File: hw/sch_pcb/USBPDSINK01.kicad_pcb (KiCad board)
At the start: 2 copper layers, 45.5 x 52.9 mm, 53 parts, among them J1 USBC_USB4105-GF-A, J2 HEADER_2x05_PARALLEL, J3 HEADER_2x04_PARALLEL, J4 HEADER_2x03_PARALLEL, J5 HEADER_2x01, J6 HEADER_2x07_PARALLEL, J7 WAGO_2604-3102, M1 HOLE, M2 HOLE, M3 HOLE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

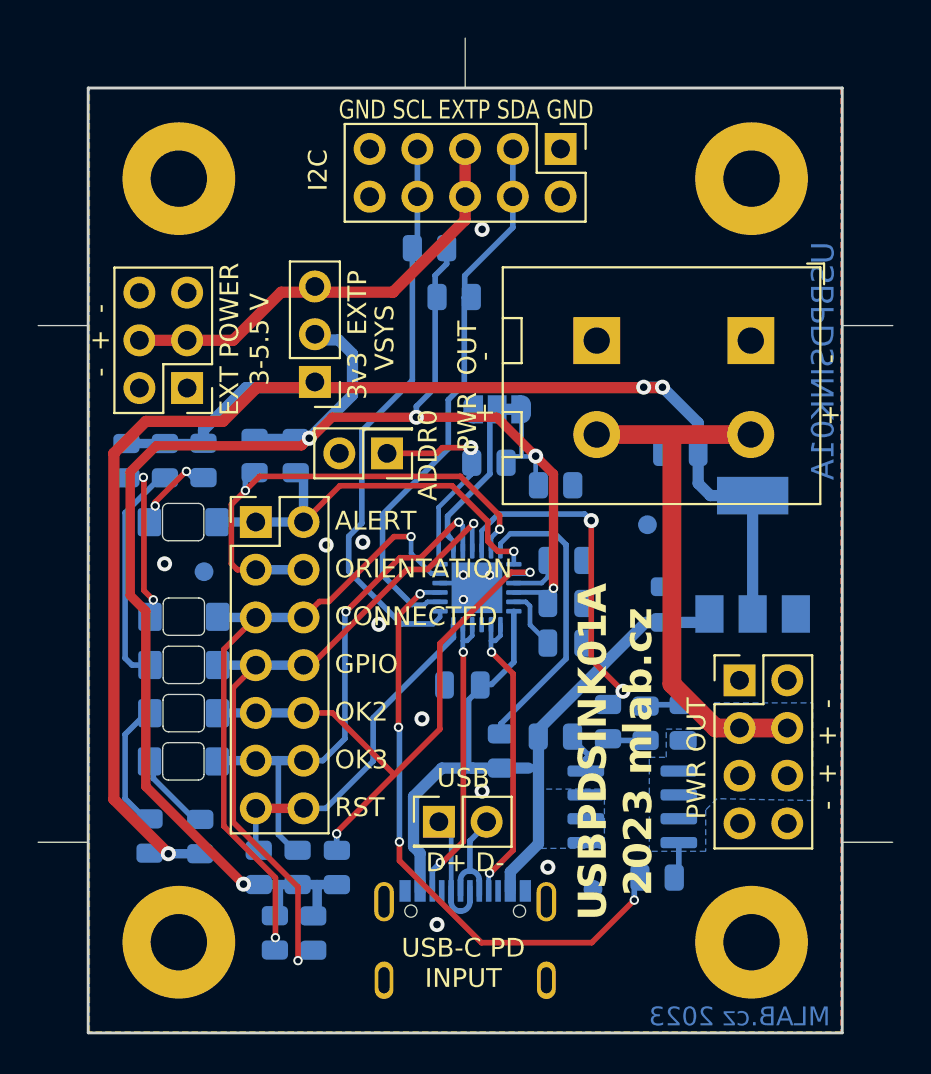
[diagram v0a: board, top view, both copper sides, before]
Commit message: add ustid, change LDO
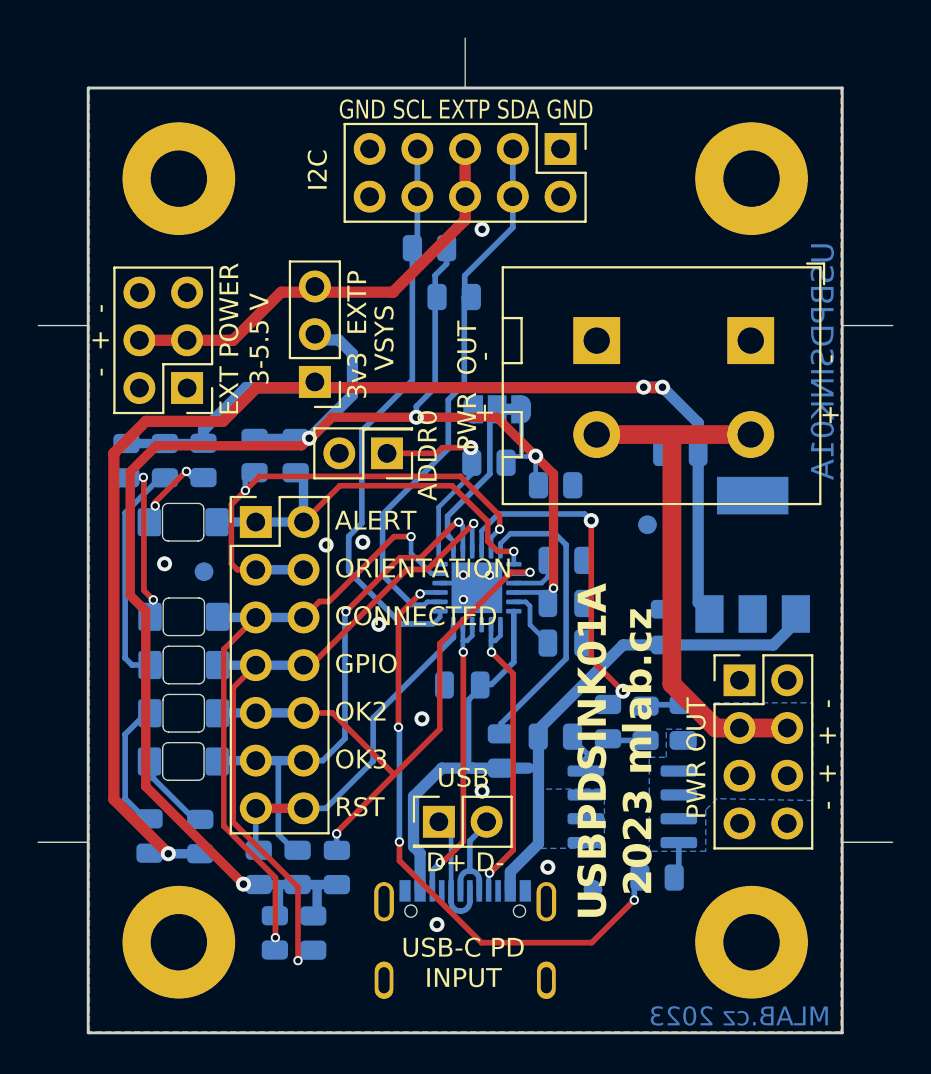
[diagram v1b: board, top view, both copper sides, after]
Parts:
- R3, R5, R6: value 65R -> 62R
- R7: value 60R -> 62R
- U2: value NCP1117-3.3 -> NCV4274CST33T3G
- moved C6 1.20 mm to (159.1, 108.5)
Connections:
- U2 pad 1: GND -> VBUS
- U2 pad 2: +3V3 -> GND
- U2 pad 3: VBUS -> +3V3
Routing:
- net VBUS: track 41.8 -> 47.1 mm
- net +3V3: track 85.3 -> 81.7 mm

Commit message: Kontrola a priprava PCB na vyrobu
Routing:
- net GND: vias 12 -> 13
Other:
- rule pad_to_mask_clearance: 0 -> 0.2
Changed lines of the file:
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@@
       (dielectric_constraints no)
     )
-    (pad_to_mask_clearance 0)
+    (pad_to_mask_clearance 0.2)
     (aux_axis_origin 123.1 135.48)
     (pcbplotparams
@@
   (via (at 141.1 104.18) (size 0.8) (drill 0.4) (layers "F.Cu" "B.Cu") (free) (net 2))
   (via (at 148.4 107.08) (size 0.5) (drill 0.3) (layers "F.Cu" "B.Cu") (net 2))
+  (via (at 149.86 107.061) (size 0.5) (drill 0.3) (layers "F.Cu" "B.Cu") (net 2))
   (via (at 148.4 105.78) (size 0.5) (drill 0.3) (layers "F.Cu" "B.Cu") (net 2))
   (via (at 149.4 117.28) (size 0.8) (drill 0.4) (layers "F.Cu" "B.Cu") (free) (net 2))
   (via (at 132.5 105.18) (size 0.8) (drill 0.4) (layers "F.Cu" "B.Cu") (free) (net 2))
   (via (at 146.2 113.43) (size 0.8) (drill 0.4) (layers "F.Cu" "B.Cu") (free) (net 2))
-  (via (at 149.8 105.78) (size 0.5) (drill 0.3) (layers "F.Cu" "B.Cu") (net 2))
+  (via (at 149.86 105.791) (size 0.5) (drill 0.3) (layers "F.Cu" "B.Cu") (net 2))
   (via (at 149.4 87.38) (size 0.8) (drill 0.4) (layers "F.Cu" "B.Cu") (free) (net 2))
   (via (at 147 124.38) (size 0.8) (drill 0.4) (layers "F.Cu" "B.Cu") (free) (net 2))
@@
   (segment (start 139.895 100.7475) (end 139.895 102.955) (width 0.5) (layer "B.Cu") (net 5))
   (segment (start 135.11 102.955) (end 139.895 102.955) (width 0.5) (layer "B.Cu") (net 5))
-  (segment (start 135.1 102.965) (end 135.11 102.955) (width 0.5) (layer "B.Cu") (net 5))
   (segment (start 151.0875 104.518) (end 151.0875 105.205) (width 0.25) (layer "B.Cu") (net 5))
   (segment (start 132 101.9) (end 133.638686 100.261314) (width 0.3) (layer "F.Cu") (net 6))
@@
   (via (at 151.9505 105.6305) (size 0.5) (drill 0.3) (layers "F.Cu" "B.Cu") (net 9))
   (segment (start 135.333332 113.115) (end 139.895 113.115) (width 0.5) (layer "B.Cu") (net 9))
-  (segment (start 141.67 120.43) (end 141.37 120.43) (width 0.3) (layer "B.Cu") (net 9))
   (segment (start 151.9505 105.6305) (end 151.876 105.705) (width 0.25) (layer "B.Cu") (net 9))
   (segment (start 135.315 113.133332) (end 135.333332 113.115) (width 0.5) (layer "B.Cu") (net 9))
@@
   (via (at 138.4 125.08) (size 0.5) (drill 0.3) (layers "F.Cu" "B.Cu") (net 13))
   (via (at 145.6182 103.7336) (size 0.5) (drill 0.3) (layers "F.Cu" "B.Cu") (net 13))
-  (segment (start 135.135 108) (end 135.17 108.035) (width 0.5) (layer "B.Cu") (net 13))
   (segment (start 138.37 125.11) (end 138.37 125.735) (width 0.3) (layer "B.Cu") (net 13))
   (segment (start 146.701992 105.705) (end 145.6182 104.621208) (width 0.25) (layer "B.Cu") (net 13))
@@
   (segment (start 140.188461 98.5075) (end 139.48 98.5075) (width 0.6) (layer "B.Cu") (net 28))
   (segment (start 142.5 94) (end 141.765 93.265) (width 0.6) (layer "B.Cu") (net 28))
-  (segment (start 147.5225 88.39) (end 147.5125 88.38) (width 0.3) (layer "B.Cu") (net 28))
   (segment (start 151.5 96.9575) (end 151.5 99.4664) (width 0.25) (layer "B.Cu") (net 28))
   (segment (start 152.25 100.75) (end 152.4 100.9) (width 0.25) (layer "B.Cu") (net 28))

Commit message: Kontrola, upravi pred vyrobou
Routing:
- net GND: vias 13 -> 14
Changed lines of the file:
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@@
   (via (at 148.4 105.78) (size 0.5) (drill 0.3) (layers "F.Cu" "B.Cu") (net 2))
   (via (at 149.4 117.28) (size 0.8) (drill 0.4) (layers "F.Cu" "B.Cu") (free) (net 2))
+  (via (at 129.921 112.1918) (size 0.8) (drill 0.4) (layers "F.Cu" "B.Cu") (free) (net 2))
   (via (at 132.5 105.18) (size 0.8) (drill 0.4) (layers "F.Cu" "B.Cu") (free) (net 2))
   (via (at 146.2 113.43) (size 0.8) (drill 0.4) (layers "F.Cu" "B.Cu") (free) (net 2))
